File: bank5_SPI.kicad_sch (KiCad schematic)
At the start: 10 parts, among them U1 NX1H35 PBGA625, U2 CY15B108QN-40SXI, U3 M95P32-IXMNT/E, U4 CY15B108QN-40SXI

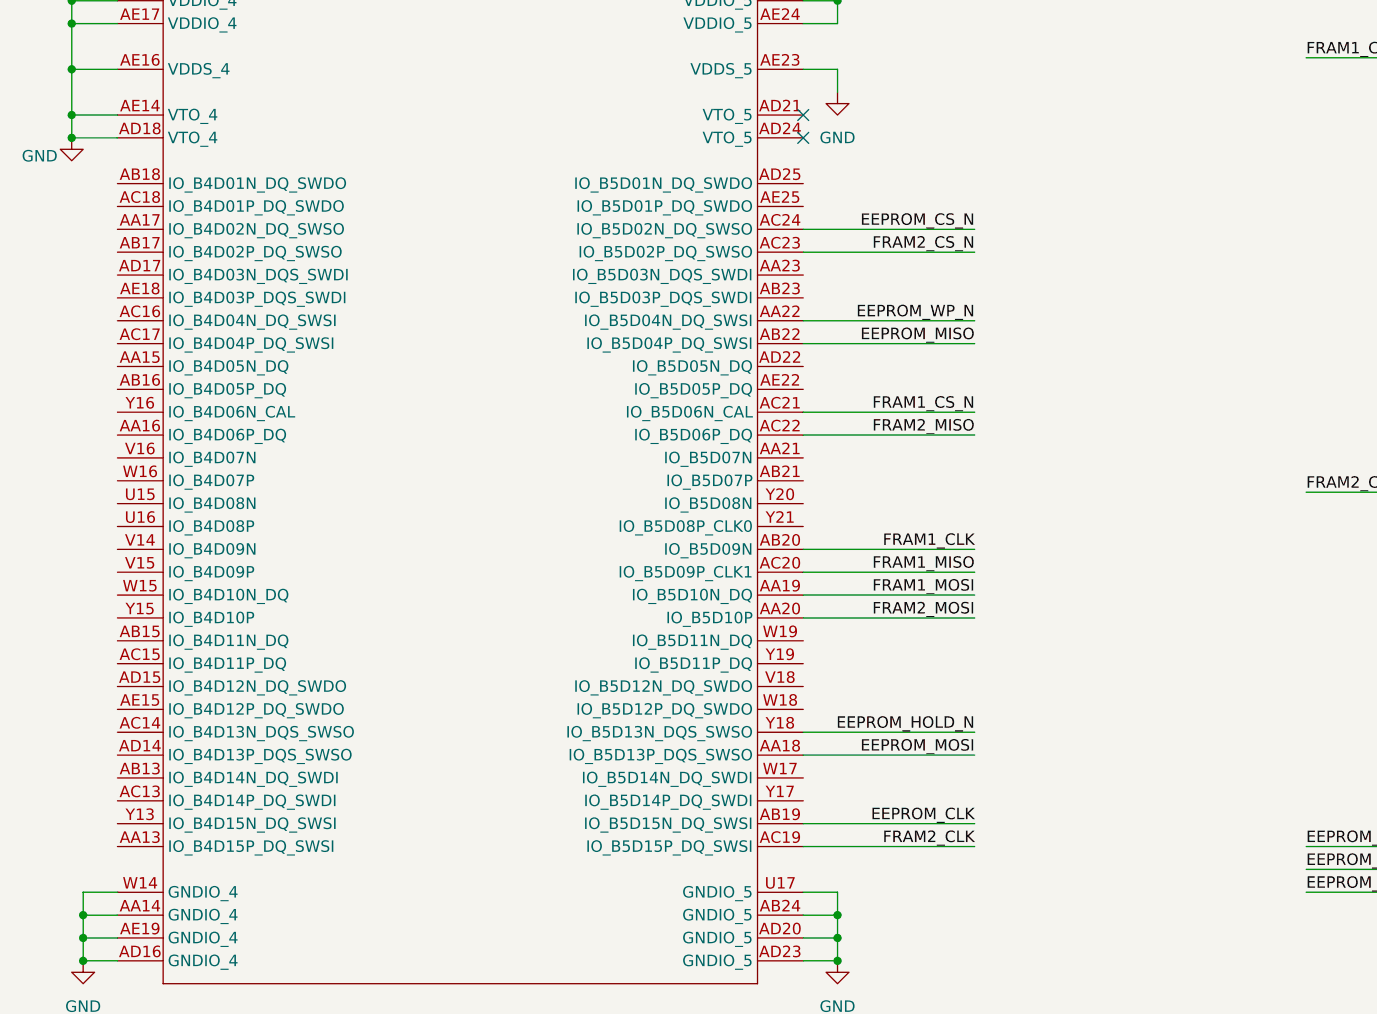
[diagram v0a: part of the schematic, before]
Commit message: SDRAM, bank5
last iteration of sdram. max optimization routing and space wise. Traced 2 frams to Bank 5. Fanout of bank 5 for DF9
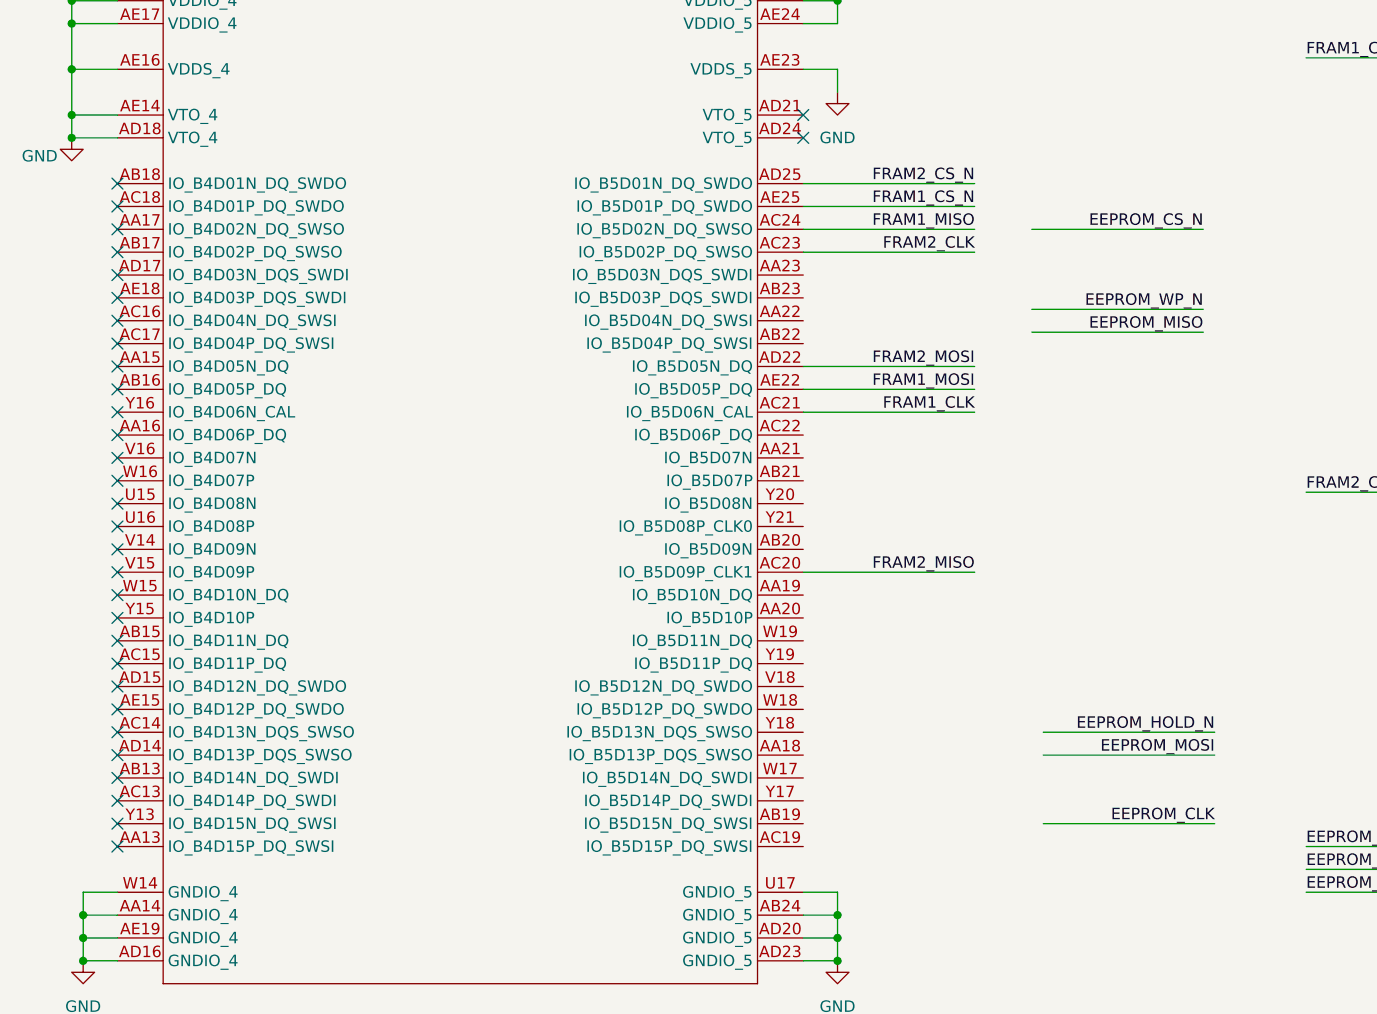
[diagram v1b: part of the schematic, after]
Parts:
- R2, R4, R5: footprint Resistor_SMD:R_0603_1608Metric_Pad0.98x0.95mm_HandSolder -> Resistor_SMD:R_0402_1005Metric_Pad0.72x0.64mm_HandSolder
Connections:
- net EEPROM_CLK: no longer U1.AB19 (IO_B5D15N_DQ_SWSI)
- net EEPROM_CS_N: no longer U1.AC24 (IO_B5D02N_DQ_SWSO)
- net EEPROM_HOLD_N: no longer U1.Y18 (IO_B5D13N_DQS_SWSO)
- net EEPROM_MISO: no longer U1.AB22 (IO_B5D04P_DQ_SWSI)
- net EEPROM_MOSI: no longer U1.AA18 (IO_B5D13P_DQS_SWSO)
- net EEPROM_WP_N: no longer U1.AA22 (IO_B5D04N_DQ_SWSI)
- net FRAM1_CLK: now also U1.AC21 (IO_B5D06N_CAL); no longer U1.AB20 (IO_B5D09N)
- net FRAM1_CS_N: now also U1.AE25 (IO_B5D01P_DQ_SWDO); no longer U1.AC21 (IO_B5D06N_CAL)
- net FRAM1_MISO: now also U1.AC24 (IO_B5D02N_DQ_SWSO); no longer U1.AC20 (IO_B5D09P_CLK1)
- net FRAM1_MOSI: now also U1.AE22 (IO_B5D05P_DQ); no longer U1.AA19 (IO_B5D10N_DQ)
- net FRAM2_CLK: now also U1.AC23 (IO_B5D02P_DQ_SWSO); no longer U1.AC19 (IO_B5D15P_DQ_SWSI)
- net FRAM2_CS_N: now also U1.AD25 (IO_B5D01N_DQ_SWDO); no longer U1.AC23 (IO_B5D02P_DQ_SWSO)
- net FRAM2_MISO: now also U1.AC20 (IO_B5D09P_CLK1); no longer U1.AC22 (IO_B5D06P_DQ)
- net FRAM2_MOSI: now also U1.AD22 (IO_B5D05N_DQ); no longer U1.AA20 (IO_B5D10P)
- no-connect marks 4 -> 34
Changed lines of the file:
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@@
+	)
+	(no_connect
+		(at 48.26 92.71)
+	)
+	(no_connect
+		(at 48.26 115.57)
 	)
 	(no_connect
@@
 	)
 	(no_connect
+		(at 48.26 118.11)
+	)
+	(no_connect
+		(at 48.26 87.63)
+	)
+	(no_connect
+		(at 48.26 72.39)
+	)
+	(no_connect
+		(at 48.26 135.89)
+	)
+	(no_connect
+		(at 48.26 128.27)
+	)
+	(no_connect
+		(at 48.26 95.25)
+	)
+	(no_connect
+		(at 48.26 138.43)
+	)
+	(no_connect
+		(at 48.26 130.81)
+	)
+	(no_connect
+		(at 48.26 74.93)
+	)
+	(no_connect
+		(at 48.26 113.03)
+	)
+	(no_connect
+		(at 48.26 77.47)
+	)
+	(no_connect
+		(at 48.26 82.55)
+	)
+	(no_connect
+		(at 48.26 140.97)
+	)
+	(no_connect
+		(at 48.26 67.31)
+	)
+	(no_connect
 		(at 201.93 45.72)
 	)
 	(no_connect
+		(at 48.26 102.87)
+	)
+	(no_connect
 		(at 124.46 62.23)
 	)
 	(no_connect
+		(at 48.26 120.65)
+	)
+	(no_connect
+		(at 48.26 133.35)
+	)
+	(no_connect
+		(at 48.26 107.95)
+	)
+	(no_connect
+		(at 48.26 123.19)
+	)
+	(no_connect
+		(at 48.26 85.09)
+	)
+	(no_connect
+		(at 48.26 90.17)
+	)
+	(no_connect
+		(at 48.26 69.85)
+	)
+	(no_connect
+		(at 48.26 97.79)
+	)
+	(no_connect
+		(at 48.26 105.41)
+	)
+	(no_connect
+		(at 48.26 125.73)
+	)
+	(no_connect
+		(at 48.26 110.49)
+	)
+	(no_connect
+		(at 48.26 80.01)
+	)
+	(no_connect
 		(at 201.93 93.98)
 	)
+	(no_connect
+		(at 48.26 100.33)
+	)
 	(wire
 		(pts
@@
 	(wire
 		(pts
-			(xy 143.51 128.27) (xy 124.46 128.27)
+			(xy 170.18 128.27) (xy 151.13 128.27)
 		)
 		(stroke
@@
 	(wire
 		(pts
-			(xy 124.46 95.25) (xy 143.51 95.25)
+			(xy 124.46 110.49) (xy 143.51 110.49)
 		)
 		(stroke
@@
 	(wire
 		(pts
-			(xy 124.46 107.95) (xy 143.51 107.95)
+			(xy 124.46 92.71) (xy 143.51 92.71)
 		)
 		(stroke
@@
 	(wire
 		(pts
-			(xy 124.46 115.57) (xy 143.51 115.57)
+			(xy 124.46 87.63) (xy 143.51 87.63)
 		)
 		(stroke
@@
 	(wire
 		(pts
-			(xy 143.51 72.39) (xy 124.46 72.39)
+			(xy 168.91 72.39) (xy 149.86 72.39)
 		)
 		(stroke
@@
 	(wire
 		(pts
-			(xy 124.46 140.97) (xy 143.51 140.97)
-		)
-		(stroke
-			(width 0)
-			(type default)
-		)
-	)
-	(wire
-		(pts
-			(xy 124.46 92.71) (xy 143.51 92.71)
+			(xy 124.46 74.93) (xy 143.51 74.93)
+		)
+		(stroke
+			(width 0)
+			(type default)
+		)
+	)
+	(wire
+		(pts
+			(xy 124.46 69.85) (xy 143.51 69.85)
 		)
 		(stroke
@@
 	(wire
 		(pts
-			(xy 124.46 138.43) (xy 143.51 138.43)
-		)
-		(stroke
-			(width 0)
-			(type default)
-		)
-	)
-	(wire
-		(pts
-			(xy 124.46 130.81) (xy 143.51 130.81)
+			(xy 151.13 138.43) (xy 170.18 138.43)
+		)
+		(stroke
+			(width 0)
+			(type default)
+		)
+	)
+	(wire
+		(pts
+			(xy 151.13 130.81) (xy 170.18 130.81)
 		)
 		(stroke
@@
 	(wire
 		(pts
-			(xy 124.46 85.09) (xy 143.51 85.09)
+			(xy 149.86 83.82) (xy 168.91 83.82)
 		)
 		(stroke
@@
 	(wire
 		(pts
-			(xy 124.46 113.03) (xy 143.51 113.03)
+			(xy 124.46 90.17) (xy 143.51 90.17)
 		)
 		(stroke
@@
 	(wire
 		(pts
-			(xy 124.46 110.49) (xy 143.51 110.49)
+			(xy 124.46 72.39) (xy 143.51 72.39)
 		)
 		(stroke
@@
 	(wire
 		(pts
-			(xy 124.46 74.93) (xy 143.51 74.93)
+			(xy 124.46 67.31) (xy 143.51 67.31)
 		)
 		(stroke
@@
 	(wire
 		(pts
-			(xy 143.51 82.55) (xy 124.46 82.55)
+			(xy 168.91 81.28) (xy 149.86 81.28)
 		)
 		(stroke
@@
 	)
 	(label "EEPROM_MISO"
-		(at 143.51 85.09 180)
+		(at 168.91 83.82 180)
 		(effects
 			(font
@@
 	)
 	(label "FRAM1_CLK"
-		(at 143.51 107.95 180)
+		(at 143.51 92.71 180)
 		(effects
 			(font
@@
 	)
 	(label "FRAM1_MOSI"
-		(at 143.51 113.03 180)
+		(at 143.51 90.17 180)
 		(effects
 			(font
@@
 	)
 	(label "EEPROM_WP_N"
-		(at 143.51 82.55 180)
+		(at 168.91 81.28 180)
 		(effects
 			(font
@@
 	)
 	(label "FRAM2_MOSI"
-		(at 143.51 115.57 180)
+		(at 143.51 87.63 180)
 		(effects
 			(font
@@
 	)
 	(label "FRAM2_CS_N"
-		(at 143.51 74.93 180)
+		(at 143.51 67.31 180)
 		(effects
 			(font
@@
 	)
 	(label "FRAM2_MISO"
-		(at 143.51 95.25 180)
+		(at 143.51 110.49 180)
 		(effects
 			(font
@@
 	)
 	(label "FRAM2_CLK"
-		(at 143.51 140.97 180)
+		(at 143.51 74.93 180)
 		(effects
 			(font
@@
 	)
 	(label "FRAM1_CS_N"
-		(at 143.51 92.71 180)
+		(at 143.51 69.85 180)
 		(effects
 			(font
@@
 	)
 	(label "EEPROM_CLK"
-		(at 143.51 138.43 180)
+		(at 170.18 138.43 180)
 		(effects
 			(font
@@
 	)
 	(label "EEPROM_CS_N"
-		(at 143.51 72.39 180)
+		(at 168.91 72.39 180)
 		(effects
 			(font
@@
 	)
 	(label "FRAM1_MISO"
-		(at 143.51 110.49 180)
+		(at 143.51 72.39 180)
 		(effects
 			(font
@@
 	)
 	(label "EEPROM_MOSI"
-		(at 143.51 130.81 180)
+		(at 170.18 130.81 180)
 		(effects
 			(font
@@
 	)
 	(label "EEPROM_HOLD_N"
-		(at 143.51 128.27 180)
+		(at 170.18 128.27 180)
 		(effects
 			(font
@@
 			)
 		)
-		(property "Footprint" "Resistor_SMD:R_0603_1608Metric_Pad0.98x0.95mm_HandSolder"
+		(property "Footprint" "Resistor_SMD:R_0402_1005Metric_Pad0.72x0.64mm_HandSolder"
 			(at 198.12 134.62 0)
 			(effects
@@
 			)
 		)
-		(property "Footprint" "Resistor_SMD:R_0603_1608Metric_Pad0.98x0.95mm_HandSolder"
+		(property "Footprint" "Resistor_SMD:R_0402_1005Metric_Pad0.72x0.64mm_HandSolder"
 			(at 196.85 93.98 0)
 			(effects
@@
 			)
 		)
-		(property "Footprint" "Resistor_SMD:R_0603_1608Metric_Pad0.98x0.95mm_HandSolder"
+		(property "Footprint" "Resistor_SMD:R_0402_1005Metric_Pad0.72x0.64mm_HandSolder"
 			(at 196.85 45.72 0)
 			(effects

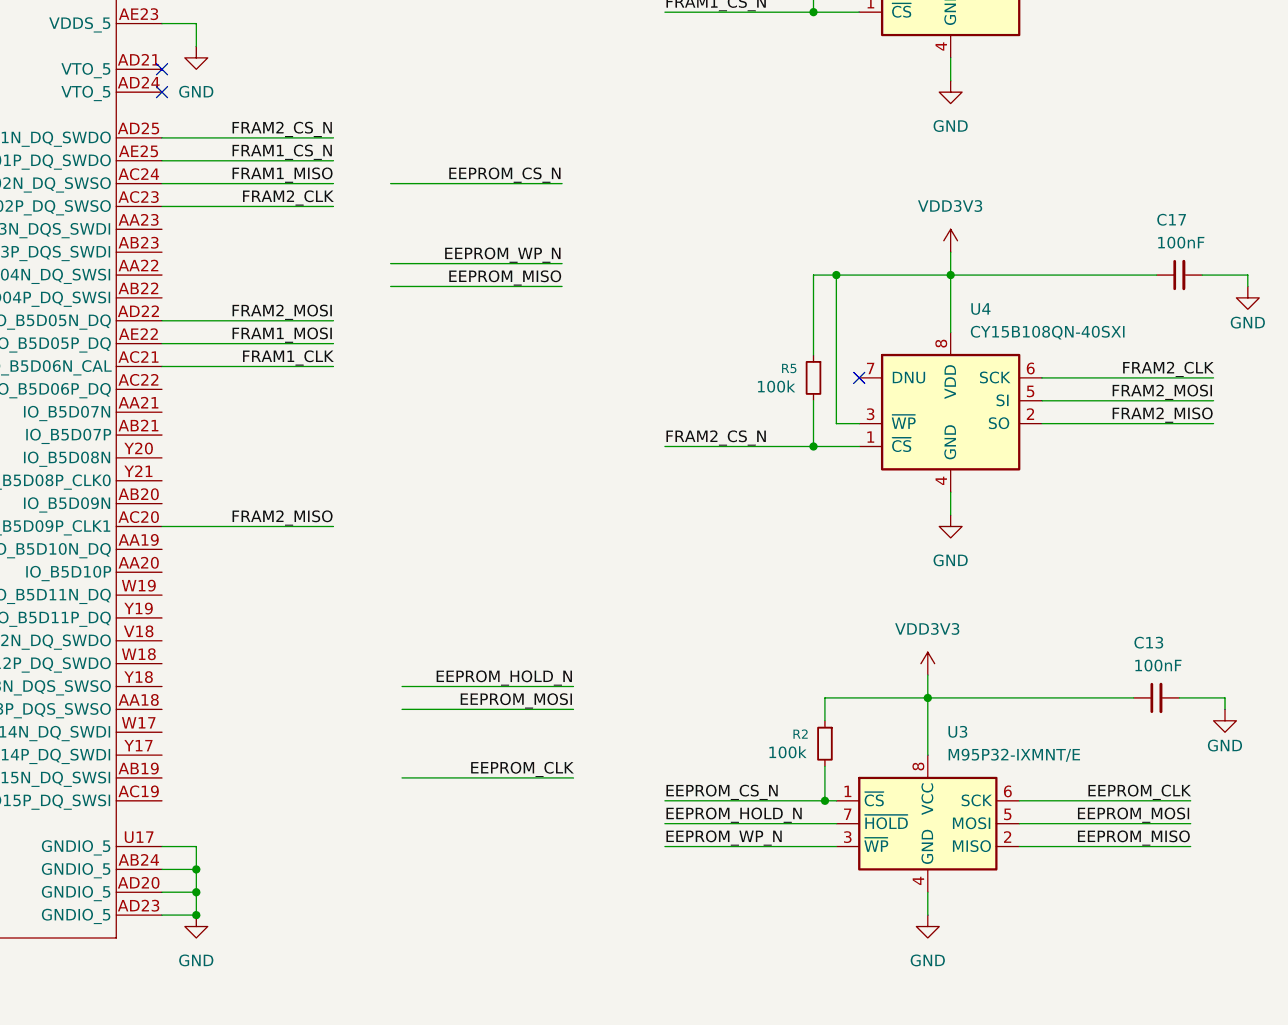
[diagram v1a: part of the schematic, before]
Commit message: full components, LEDS, changed edges
all components on pcb editor. added and  routed leds and 2 PLL. changed edges o have more space
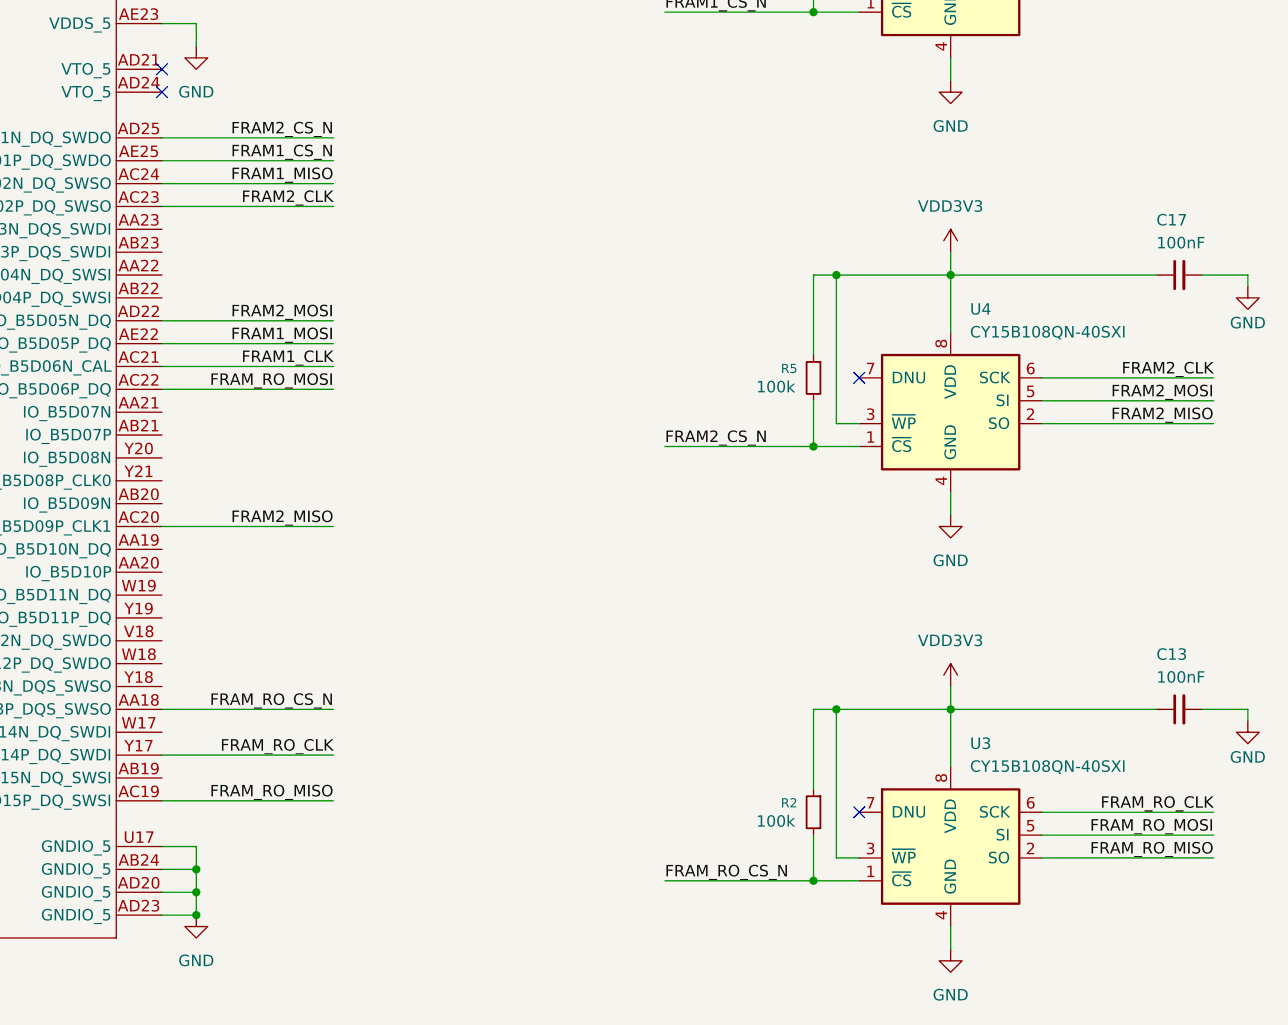
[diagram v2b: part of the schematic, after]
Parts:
- removed U3: M95P32-IXMNT/E, DataHub_Footprints:SO8N_4X5X1P27_STM, symbol Memory_EEPROM:25LCxxx-MF
- added U3: CY15B108QN-40SXI, DataHub_Footprints:SOIC8_001-85261_CYP, symbol Memory_NVRAM:MB85RS1MT
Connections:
- net EEPROM_CS_N is gone; now on net FRAM_RO_CS_N: R2.2
- net GND: now also U3.4 (GND)
- net VDD3V3: now also U3.3 (~{WP}), U3.8 (VDD)
- net FRAM_RO_CS_N: now reaches U1.AA18 (IO_B5D13P_DQS_SWSO)
- net FRAM_RO_CS_N: now also U3.1 (~{CS})
- net FRAM_RO_MISO: now reaches U1.AC19 (IO_B5D15P_DQ_SWSI)
- net FRAM_RO_MISO: now also U3.2 (SO)
- net FRAM_RO_MOSI: now reaches U1.AC22 (IO_B5D06P_DQ)
- net FRAM_RO_MOSI: now also U3.5 (SI)
- net FRAM_RO_CLK: now reaches U1.Y17 (IO_B5D14P_DQ_SWDI)
- net FRAM_RO_CLK: now also U3.6 (SCK)
- no-connect marks 34 -> 35

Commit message: CFG, bga sdram, banks to connectors, docoupling
Finished completely routing bga sdram, finished tracing Banks to connectors DF9. Finished tracing Picoblade, diode, reset supervisor. Finished tracing LEDS on bank 5. Finished decoupling all banks and core. Missing only the power tree and power rail level decoupling.
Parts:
- added D10, D11, D8, D9: LED_green, LED_SMD:LED_0603_1608Metric, symbol Device:LED_Small
- added R16, R17, R18, R29: 1k, Resistor_SMD:R_0402_1005Metric_Pad0.72x0.64mm_HandSolder, symbol Device:R_Small
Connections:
- net GND: now also D10.2 (A), D11.2 (A), D8.2 (A), D9.2 (A)
- net LD_USER4: now reaches U1.AB19 (IO_B5D15N_DQ_SWSI)
- net LD_USER4: now also R29.1
- net LD_USER2: now reaches U1.AB21 (IO_B5D07P)
- net LD_USER2: now also R17.1
- net LD_USER3: now reaches U1.AB22 (IO_B5D04P_DQ_SWSI)
- net LD_USER3: now also R18.1
- net LD_USER1: now reaches U1.W17 (IO_B5D14N_DQ_SWDI)
- net LD_USER1: now also R16.1
- new net: D8.1 (K), R16.2
- new net: D9.1 (K), R17.2
- new net: D10.1 (K), R18.2
- new net: D11.1 (K), R29.2

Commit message: power tree
power tree defined. Few changes remaining but almost finalized
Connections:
- net B5_10N_DF9: now reaches U1.AA19 (IO_B5D10N_DQ)
- net B5_10P_DF9: now reaches U1.AA20 (IO_B5D10P)
- net B5_07N_DF9: now reaches U1.AA21 (IO_B5D07N)
- net B5_04N_DF9: now reaches U1.AA22 (IO_B5D04N_DQ_SWSI)
- net B5_03N_DF9: now reaches U1.AA23 (IO_B5D03N_DQS_SWDI)
- net B5_09N_DF9: now reaches U1.AB20 (IO_B5D09N)
- net B5_03P_DF9: now reaches U1.AB23 (IO_B5D03P_DQS_SWDI)
- net B5_12N_DF9: now reaches U1.V18 (IO_B5D12N_DQ_SWDO)
- net B5_12P_DF9: now reaches U1.W18 (IO_B5D12P_DQ_SWDO)
- net B5_11N_DF9: now reaches U1.W19 (IO_B5D11N_DQ)
- net B5_13N_DF9: now reaches U1.Y18 (IO_B5D13N_DQS_SWSO)
- net B5_11P_DF9: now reaches U1.Y19 (IO_B5D11P_DQ)
- net B5_08N_DF9: now reaches U1.Y20 (IO_B5D08N)
- net B5_08P_DF9: now reaches U1.Y21 (IO_B5D08P_CLK0)

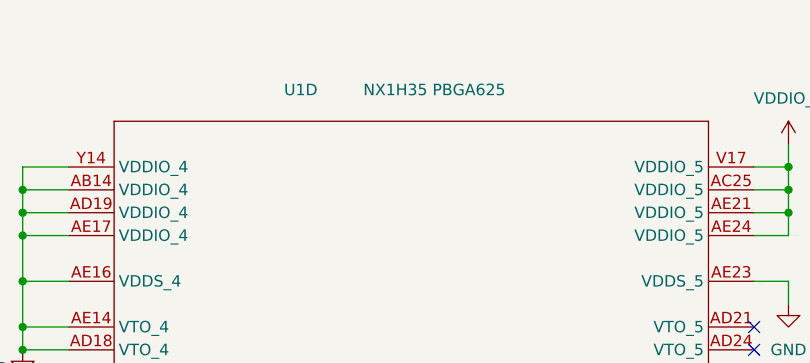
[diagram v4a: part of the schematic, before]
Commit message: finished
power planes, decoupling, ERC, DRC
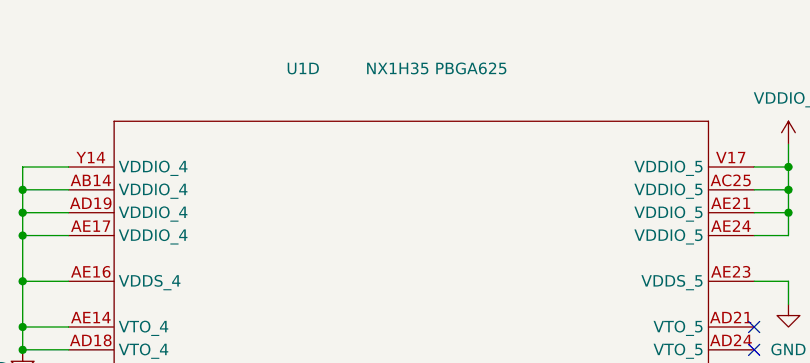
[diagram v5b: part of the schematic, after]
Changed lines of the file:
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@@
 		(dnp no)
 		(property "Reference" "U1"
-			(at 75.946 34.0868 0)
+			(at 76.2 31.75 0)
 			(effects
 				(font
@@
 		)
 		(property "Value" "NX1H35 PBGA625"
-			(at 81.026 34.0868 0)
+			(at 81.28 31.75 0)
 			(effects
 				(font
@@
 		)
 		(instances
-			(project "PCB_Project"
+			(project ""
+				(path "/ae14ff2f-b8e3-4dd1-9329-e73906805e39/77861c37-88e9-4408-9723-ec14cfd3d63b"
+					(reference "U1")
+					(unit 4)
+				)
 				(path "/ae14ff2f-b8e3-4dd1-9329-e73906805e39/b93efa78-c170-4cb6-81ef-072d5a5e973b"
 					(reference "U1")

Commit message: pre-order adjustments
DF9 connectors footprint adjusted.
Dimensions of board edges changed.
Placement of DF9 adjusted.
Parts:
- renumbered C15 to C21, C17 to C22, C13 to C23, D11 to D10, D8 to D7, D9 to D8, D10 to D9, R16 to R12, R17 to R13, R18 to R14, R29 to R15, R4 to R16, R5 to R17, R2 to R18, U2 to U5, U4 to U6, U3 to U7
